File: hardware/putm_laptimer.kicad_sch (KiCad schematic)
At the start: 49 parts, among them J1 Conn_01x22, J2 Conn_01x22, J3 Conn_01x22, J4 Conn_01x22, J5 2091-1372, J6 2091-1372, J7 Conn_02x05_Odd_Even, J8 Conn_01x09, SW1 SW_Push, SW2 SW_Push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

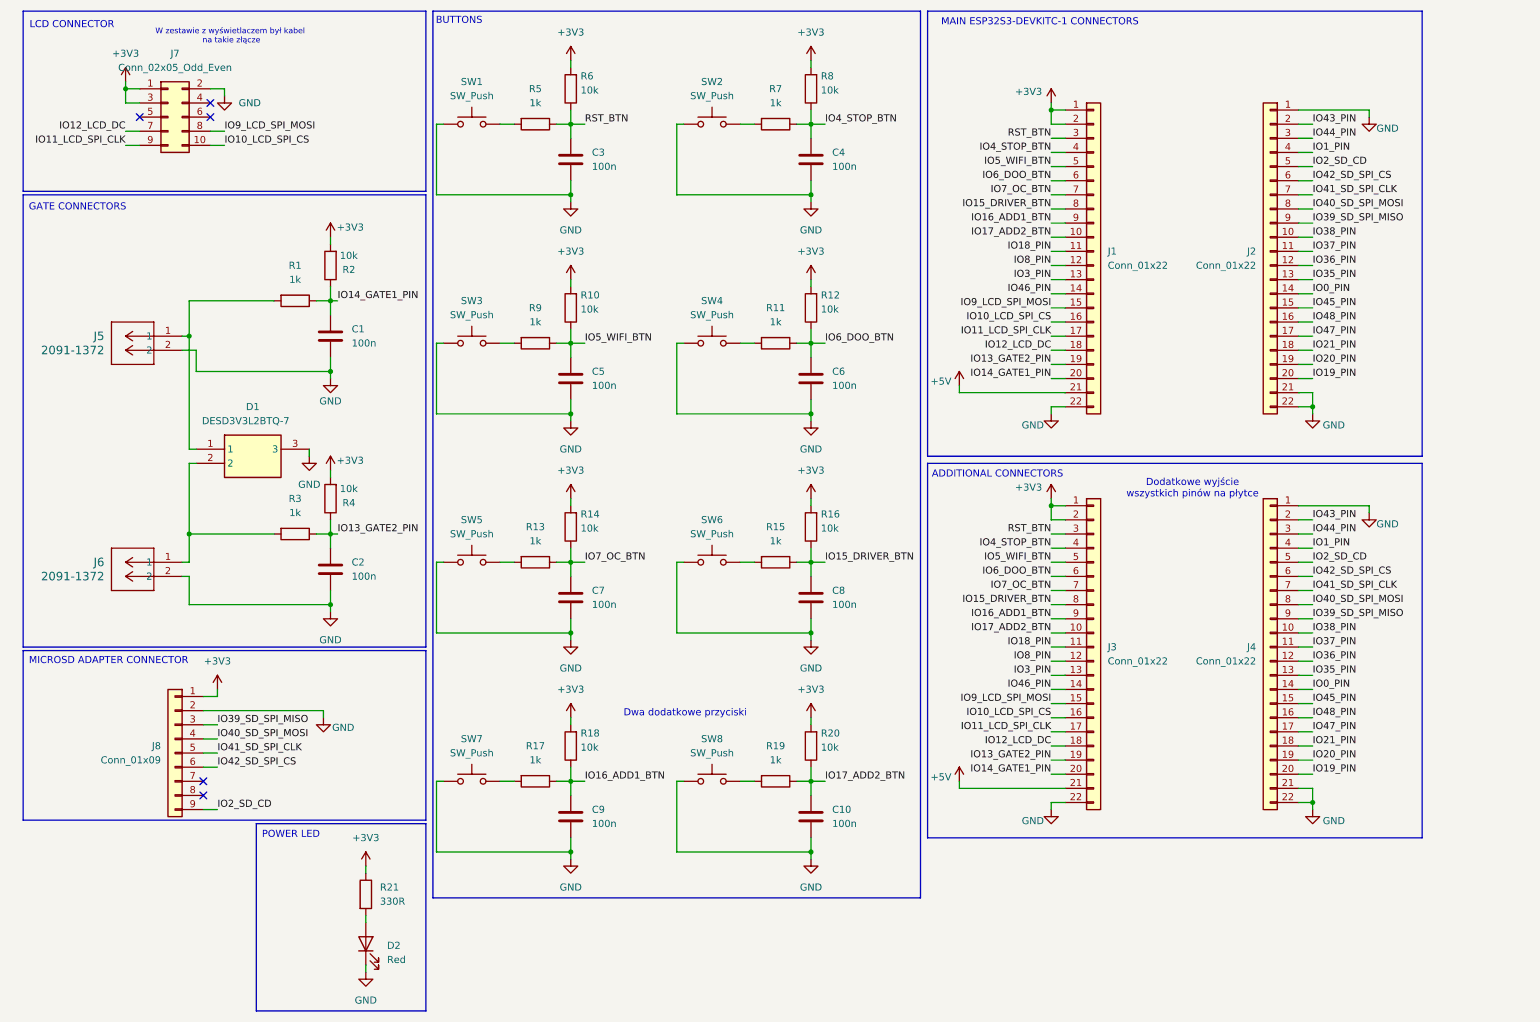
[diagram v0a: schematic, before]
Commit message: deleted buttons on board and added hawrin connector
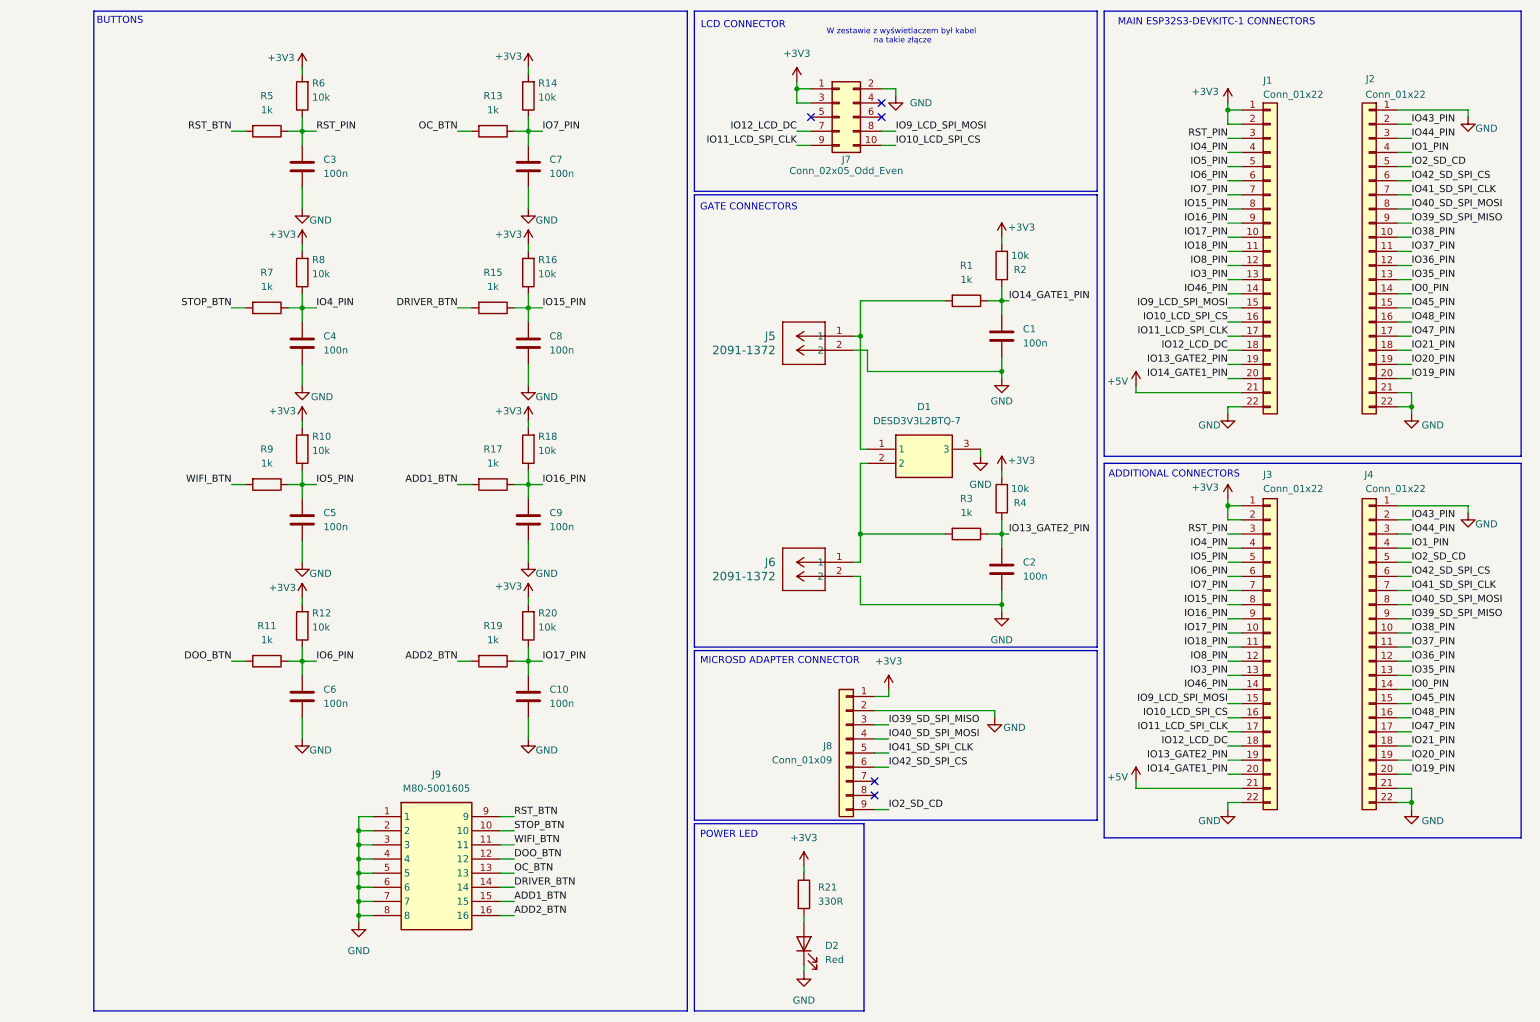
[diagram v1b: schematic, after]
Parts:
- removed SW1, SW2, SW3, SW4, SW5, SW6, SW7, SW8: SW_Push, Button_Switch_SMD:SW_Push_1P1T_NO_CK_KSC6xxG, symbol Switch:SW_Push
- added J9: M80-5001605, Footprint:M80-50016YY_2, symbol M80-5001605:M80-5001605
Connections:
- net GND: now also J9.1, J9.2, J9.3, J9.4, J9.5, J9.6, J9.7, J9.8
- net RST_BTN: now also R5.2, J9.9; no longer C3.1, J1.3 (Pin_3), J3.3 (Pin_3), R5.1, R6.1
- net ADD1_BTN: now reaches R17.2
- net ADD1_BTN: now also J9.15
- net DOO_BTN: now reaches R11.2
- net DOO_BTN: now also J9.12
- net OC_BTN: now reaches R13.2
- net OC_BTN: now also J9.13
- net ADD2_BTN: now reaches R19.2
- net ADD2_BTN: now also J9.16
- net STOP_BTN: now reaches R7.2
- net STOP_BTN: now also J9.10
- net DRIVER_BTN: now reaches R15.2
- net DRIVER_BTN: now also J9.14
- net WIFI_BTN: now reaches R9.2
- net WIFI_BTN: now also J9.11
- net IO15_DRIVER_BTN renamed IO15_PIN
- net IO16_ADD1_BTN renamed IO16_PIN
- net IO17_ADD2_BTN renamed IO17_PIN
- net IO4_STOP_BTN renamed IO4_PIN
- net IO5_WIFI_BTN renamed IO5_PIN
- net IO6_DOO_BTN renamed IO6_PIN
- net IO7_OC_BTN renamed IO7_PIN
- new net RST_PIN: C3.1, J1.3 (Pin_3), J3.3 (Pin_3), R5.1, R6.1
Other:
- note removed: "Dodatkowe wyjście wszystkich pinów na płytce"
- note removed: "Dwa dodatkowe przyciski"
- moved on the sheet: C1, C10, C2, C3, C4, C5, C6, C7, C8, C9, D1, D2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

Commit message: added rtc connectors to schematics
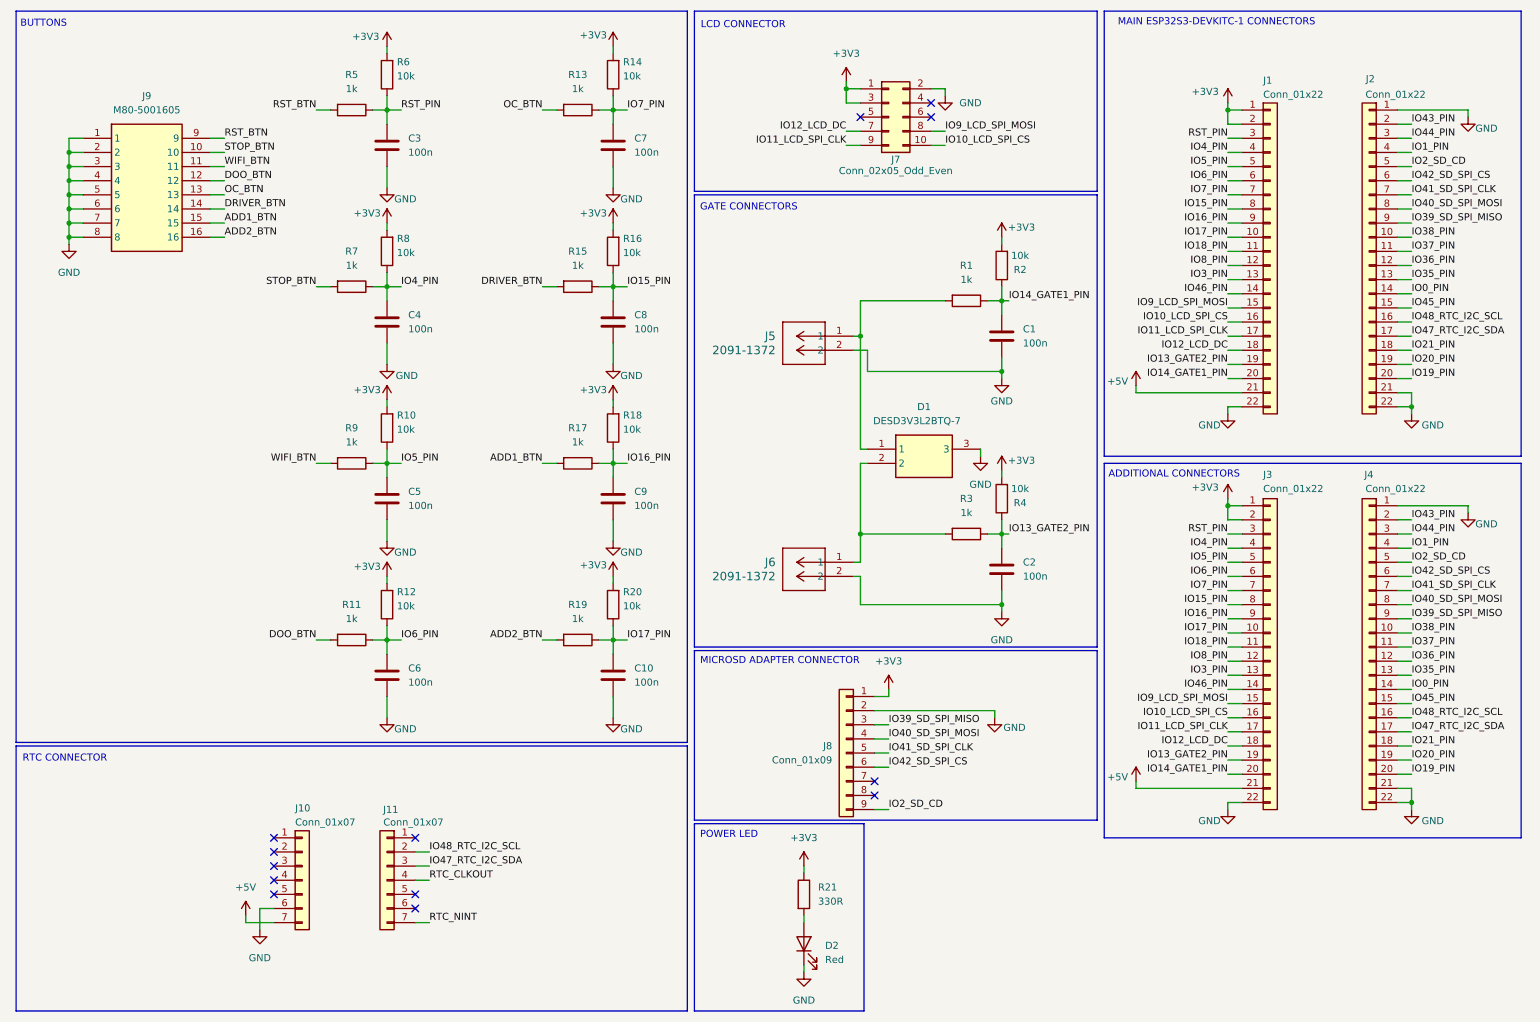
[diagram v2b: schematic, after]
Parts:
- added J10, J11: Conn_01x07, symbol Connector_Generic:Conn_01x07
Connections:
- net +5V: now also J10.7 (Pin_7)
- net GND: now also J10.6 (Pin_6)
- net IO47_PIN renamed IO47_RTC_I2C_SDA
- net IO47_RTC_I2C_SDA: now also J11.3 (Pin_3)
- net IO48_PIN renamed IO48_RTC_I2C_SCL
- net IO48_RTC_I2C_SCL: now also J11.2 (Pin_2)
- new net RTC_CLKOUT: J11.4 (Pin_4)
- new net RTC_NINT: J11.7 (Pin_7)
- no-connect marks 5 -> 13
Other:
- note added: "RTC CONNECTOR"
- note removed: "W zestawie z wyświetlaczem był kabel na takie złącze"
- moved on the sheet: C10, C3, C4, C5, C6, C7, C8, C9, J7, J9, R10, R11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

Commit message: placed rtc connectors on pcb
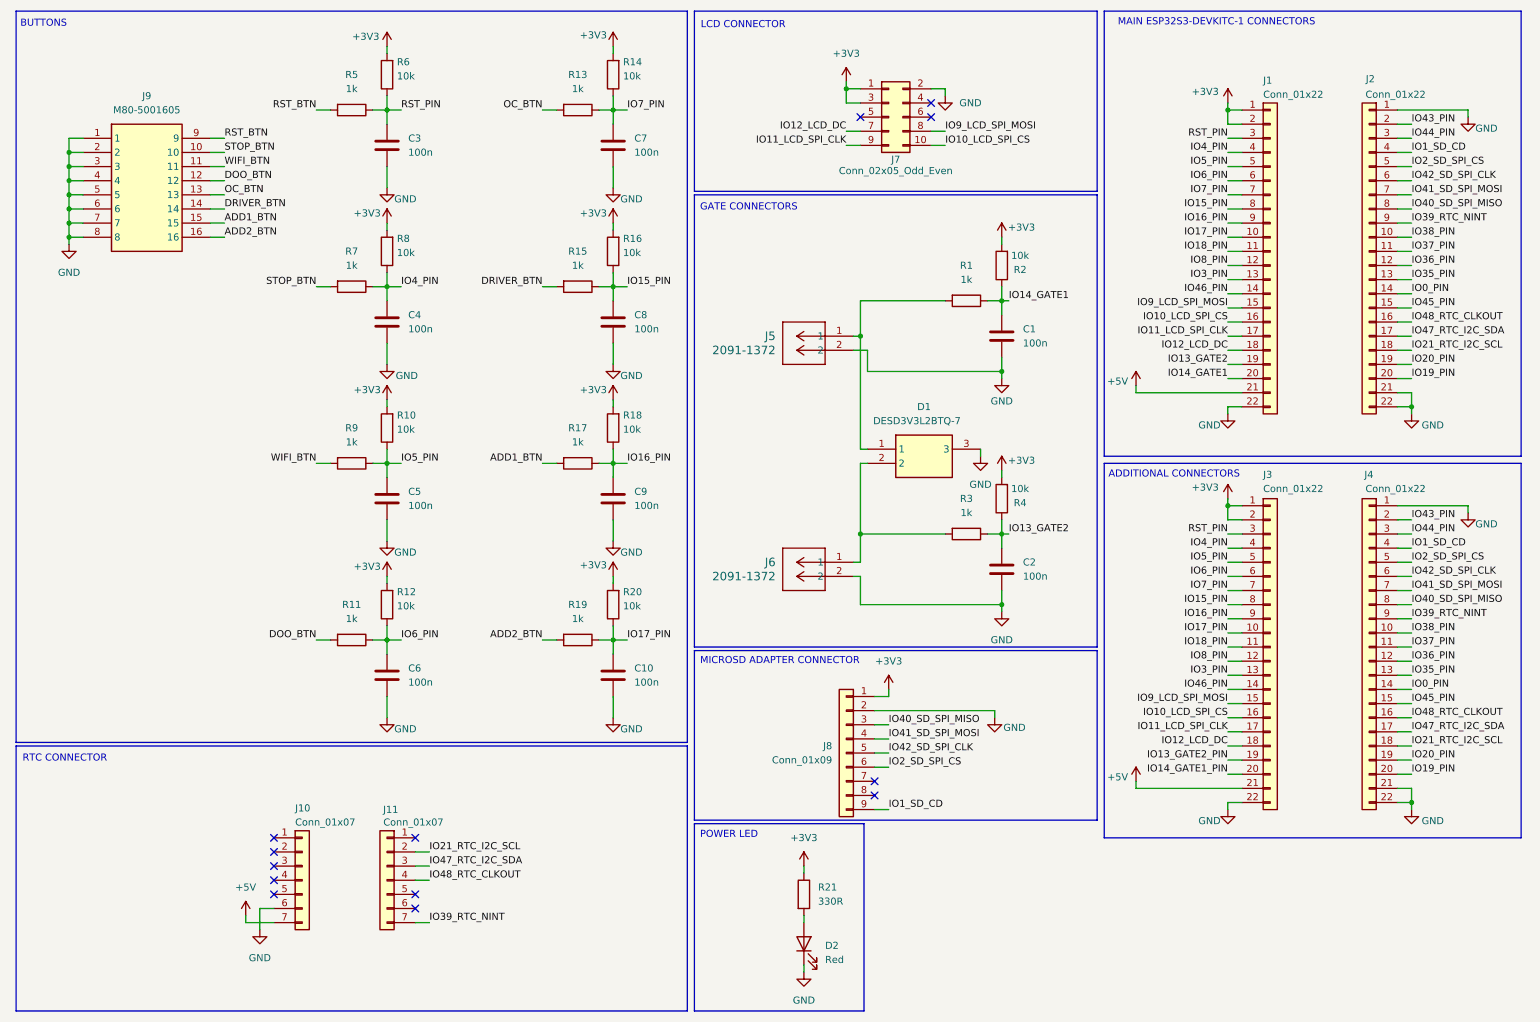
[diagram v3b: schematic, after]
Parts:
- J10, J11: footprint (none) -> Connector_PinSocket_2.54mm:PinSocket_1x07_P2.54mm_Vertical
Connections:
- net RTC_CLKOUT is gone; now on net IO48_RTC_CLKOUT: J11.4 (Pin_4)
- net RTC_NINT is gone; now on net IO39_RTC_NINT: J11.7 (Pin_7)
- net IO13_GATE2_PIN: no longer C2.1, J1.19 (Pin_19), R3.1, R4.1
- net IO14_GATE1_PIN: no longer C1.1, J1.20 (Pin_20), R1.1, R2.1
- net IO1_PIN renamed IO1_SD_CD
- net IO1_SD_CD: now also J8.9 (Pin_9)
- net IO21_PIN renamed IO21_RTC_I2C_SCL
- net IO21_RTC_I2C_SCL: now also J11.2 (Pin_2)
- net IO2_SD_CD renamed IO2_SD_SPI_CS
- net IO2_SD_SPI_CS: now also J8.6 (Pin_6); no longer J8.9 (Pin_9)
- net IO39_SD_SPI_MISO renamed IO39_RTC_NINT
- net IO39_RTC_NINT: no longer J8.3 (Pin_3)
- net IO40_SD_SPI_MOSI renamed IO40_SD_SPI_MISO
- net IO40_SD_SPI_MISO: now also J8.3 (Pin_3); no longer J8.4 (Pin_4)
- net IO41_SD_SPI_CLK renamed IO41_SD_SPI_MOSI
- net IO41_SD_SPI_MOSI: now also J8.4 (Pin_4); no longer J8.5 (Pin_5)
- net IO42_SD_SPI_CS renamed IO42_SD_SPI_CLK
- net IO42_SD_SPI_CLK: now also J8.5 (Pin_5); no longer J8.6 (Pin_6)
- net IO48_RTC_I2C_SCL renamed IO48_RTC_CLKOUT
- net IO48_RTC_CLKOUT: no longer J11.2 (Pin_2)
- new net IO13_GATE2: C2.1, J1.19 (Pin_19), R3.1, R4.1
- new net IO14_GATE1: C1.1, J1.20 (Pin_20), R1.1, R2.1

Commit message: changed harwin connector to connect power led, updated cleareance and net width
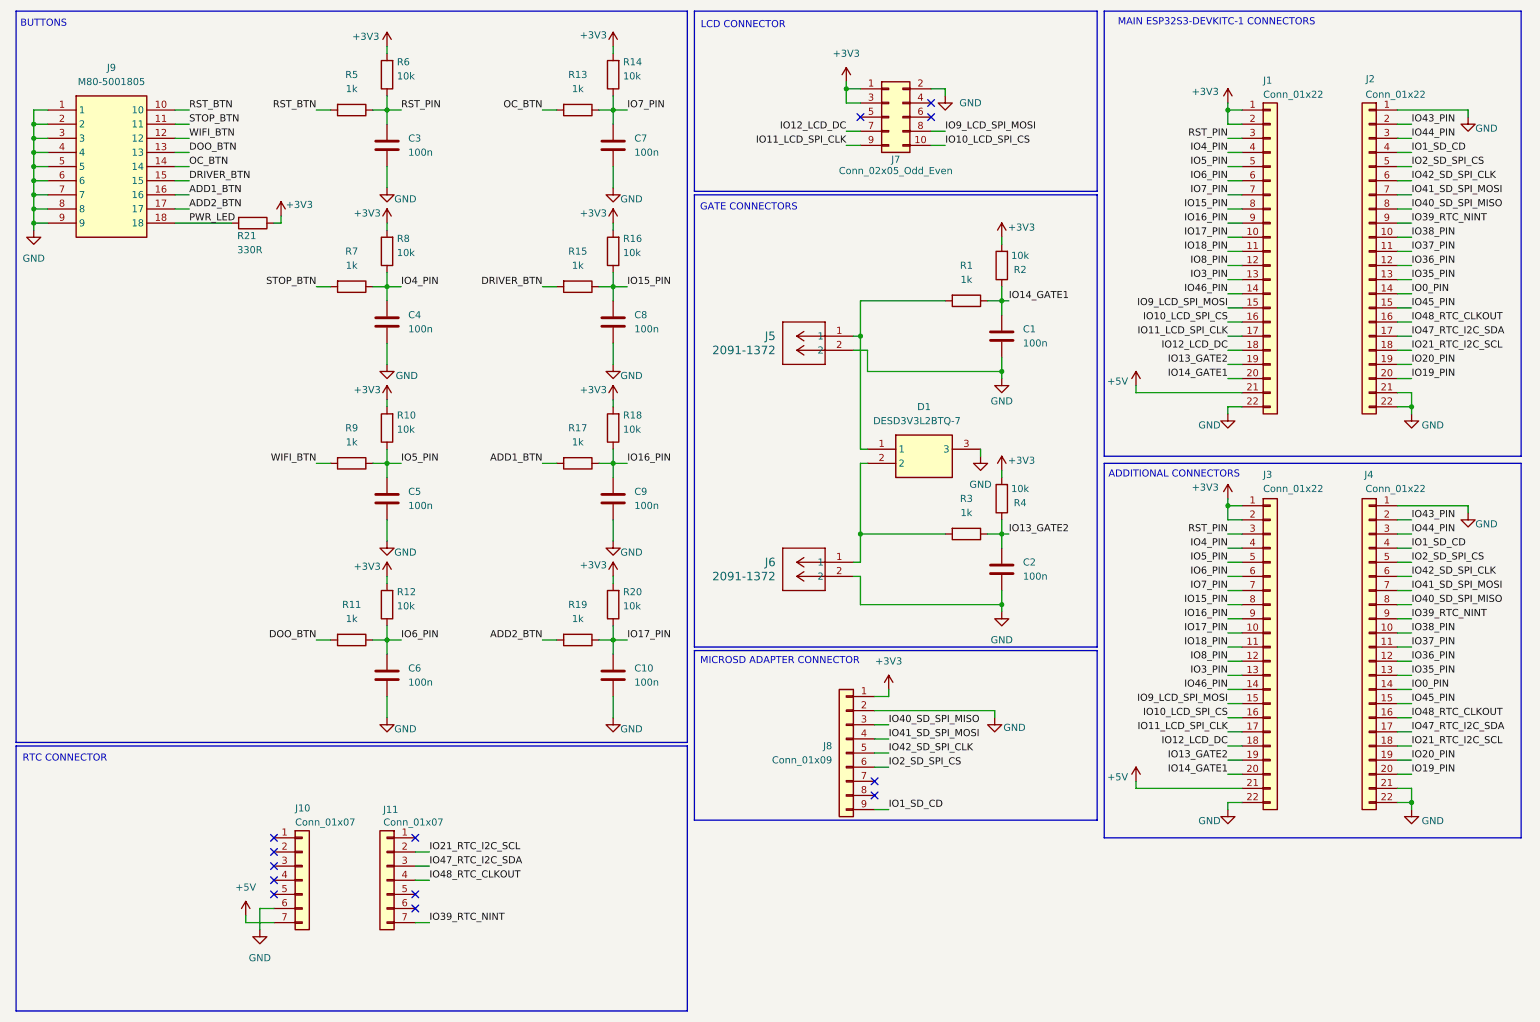
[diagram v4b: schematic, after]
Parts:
- removed D2: Red, LED_SMD:LED_0603_1608Metric, symbol Device:LED
- removed J9: M80-5001605, Footprint:M80-50016YY_2, symbol M80-5001605:M80-5001605
- added J9: M80-5001805, Footprint:M80-50018YY_2, symbol M80-5001805:M80-5001805
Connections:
- net IO13_GATE2_PIN is gone; now on net IO13_GATE2: J3.19 (Pin_19)
- net IO14_GATE1_PIN is gone; now on net IO14_GATE1: J3.20 (Pin_20)
- net ADD1_BTN: now also J9.16
- net ADD2_BTN: now also J9.17
- net DOO_BTN: now also J9.13
- net DRIVER_BTN: now also J9.15
- net GND: now also J9.1, J9.2, J9.3, J9.4, J9.5, J9.6, J9.7, J9.8, J9.9
- net OC_BTN: now also J9.14
- net RST_BTN: now also J9.10
- net STOP_BTN: now also J9.11
- net WIFI_BTN: now also J9.12
- net PWR_LED: now reaches R21.2
- net PWR_LED: now also J9.18
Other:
- note removed: "POWER LED"
- moved on the sheet: R21
